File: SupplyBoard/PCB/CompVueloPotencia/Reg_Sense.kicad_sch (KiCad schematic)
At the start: 7 parts, among them J2 Conn_01x03

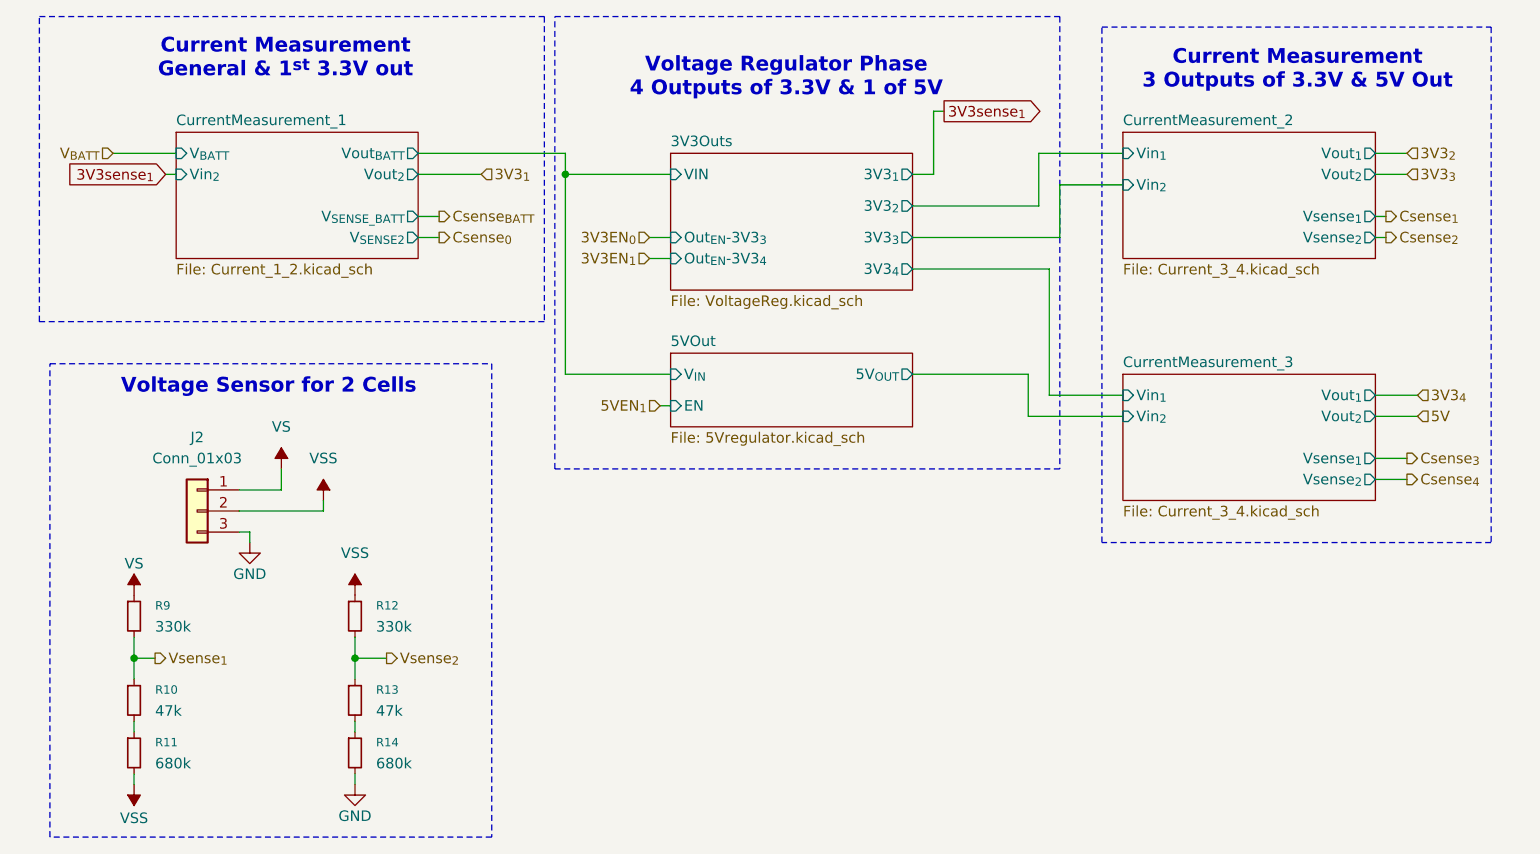
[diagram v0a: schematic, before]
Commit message: SupplyBoard - update layout
schematic completed and PCB layout started; only the routing of the traces remains to be done
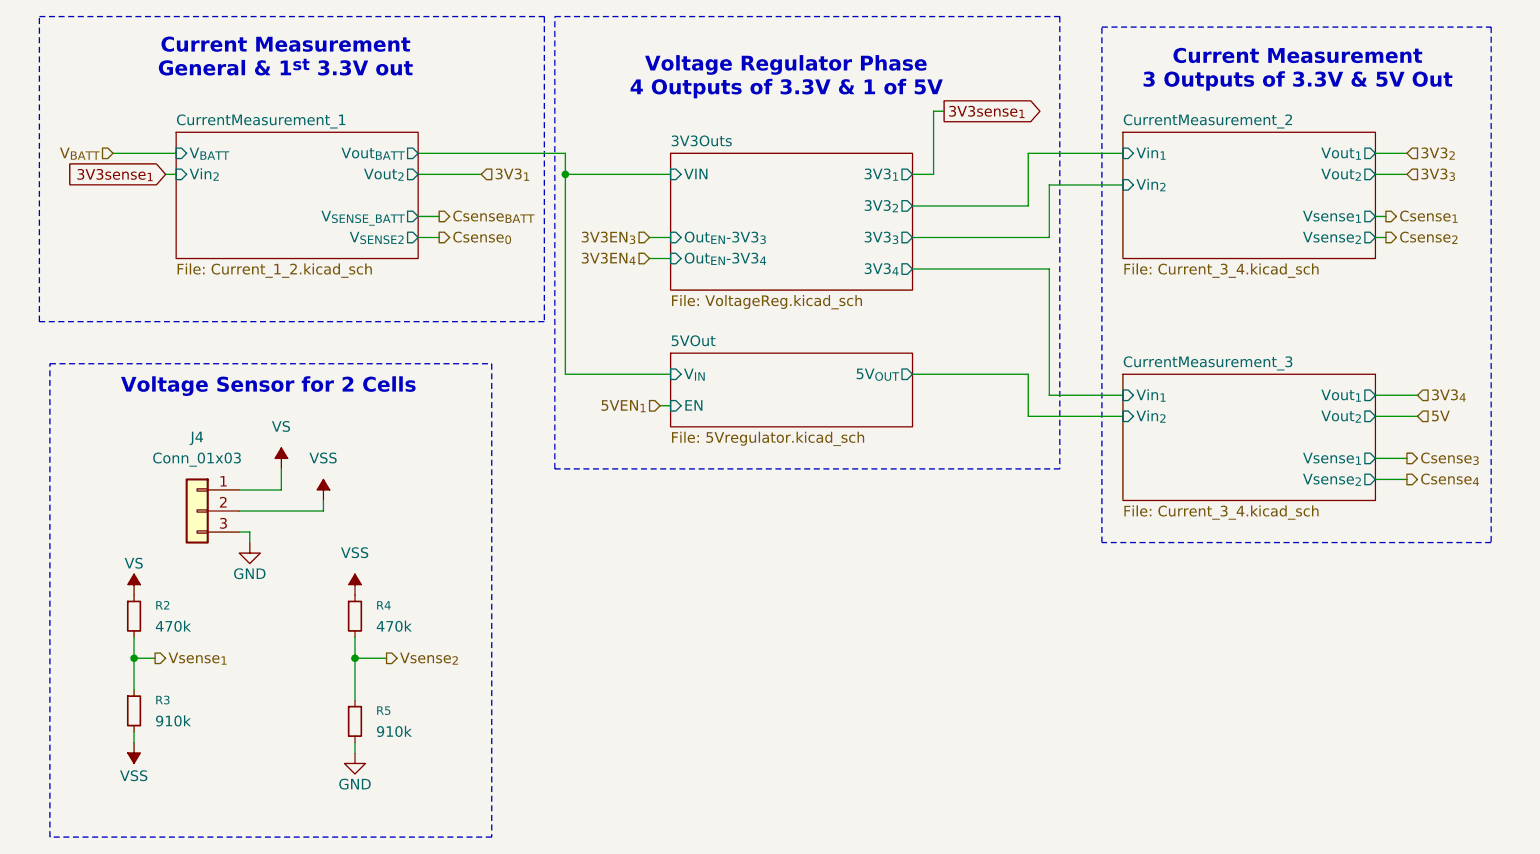
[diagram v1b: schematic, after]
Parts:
- removed R10, R13: 47k, symbol Device:R_Small
- J4: renamed from J2; footprint (none) -> Connector_PinHeader_2.54mm:PinHeader_1x03_P2.54mm_Vertical
- R2: renamed from R9; value 330k -> 470k; footprint (none) -> Resistor_SMD:R_0805_2012Metric_Pad1.20x1.40mm_HandSolder
- R3: renamed from R11; value 680k -> 910k; footprint (none) -> Resistor_SMD:R_0805_2012Metric_Pad1.20x1.40mm_HandSolder
- R4: renamed from R12; value 330k -> 470k; footprint (none) -> Resistor_SMD:R_0805_2012Metric_Pad1.20x1.40mm_HandSolder
- R5: renamed from R14; value 680k -> 910k; footprint (none) -> Resistor_SMD:R_0805_2012Metric_Pad1.20x1.40mm_HandSolder
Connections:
- net Vsense_{1}: now also R3.1
- net Vsense_{2}: now also R5.1
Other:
- moved on the sheet: R3, R5
